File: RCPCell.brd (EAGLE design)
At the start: 99.8 x 44.5 mm, 18 parts, among them IC1 SIM900, U1 PESDXS4UD

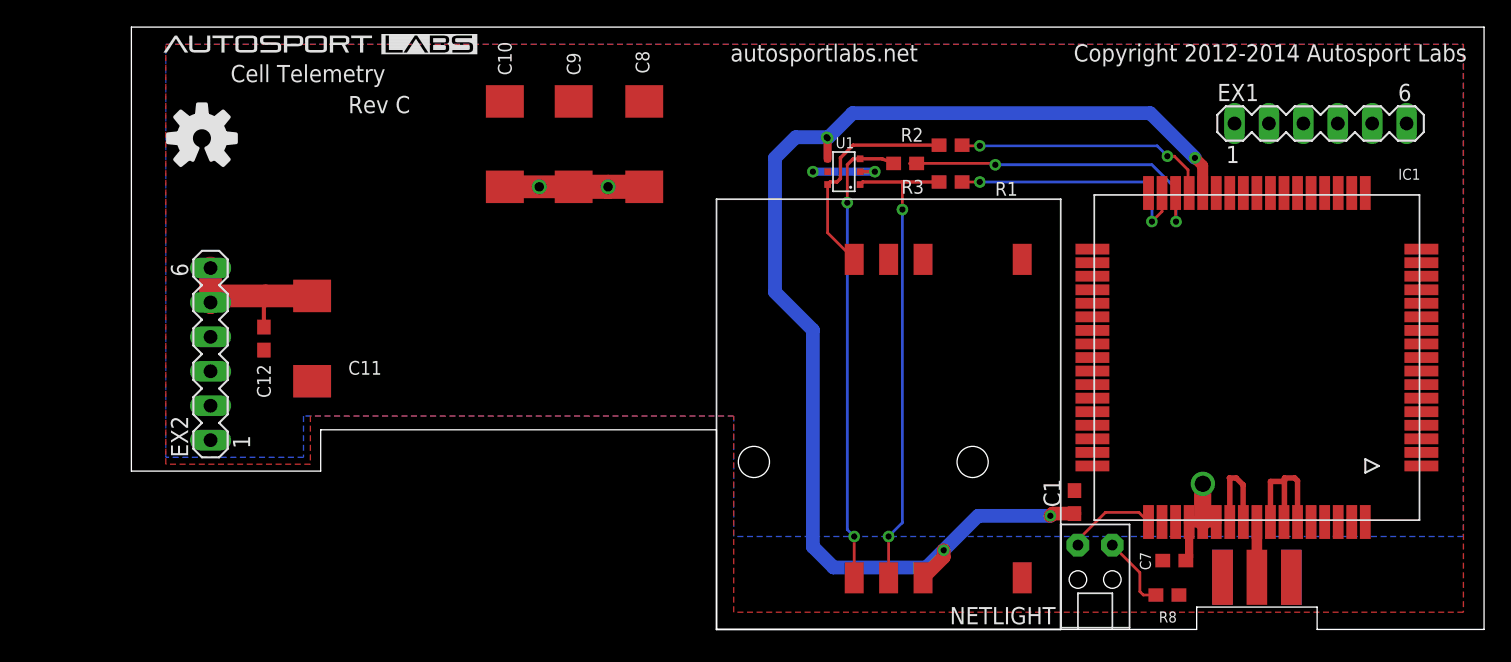
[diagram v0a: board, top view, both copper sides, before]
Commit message: laid out power supply section, fixed DRC errors
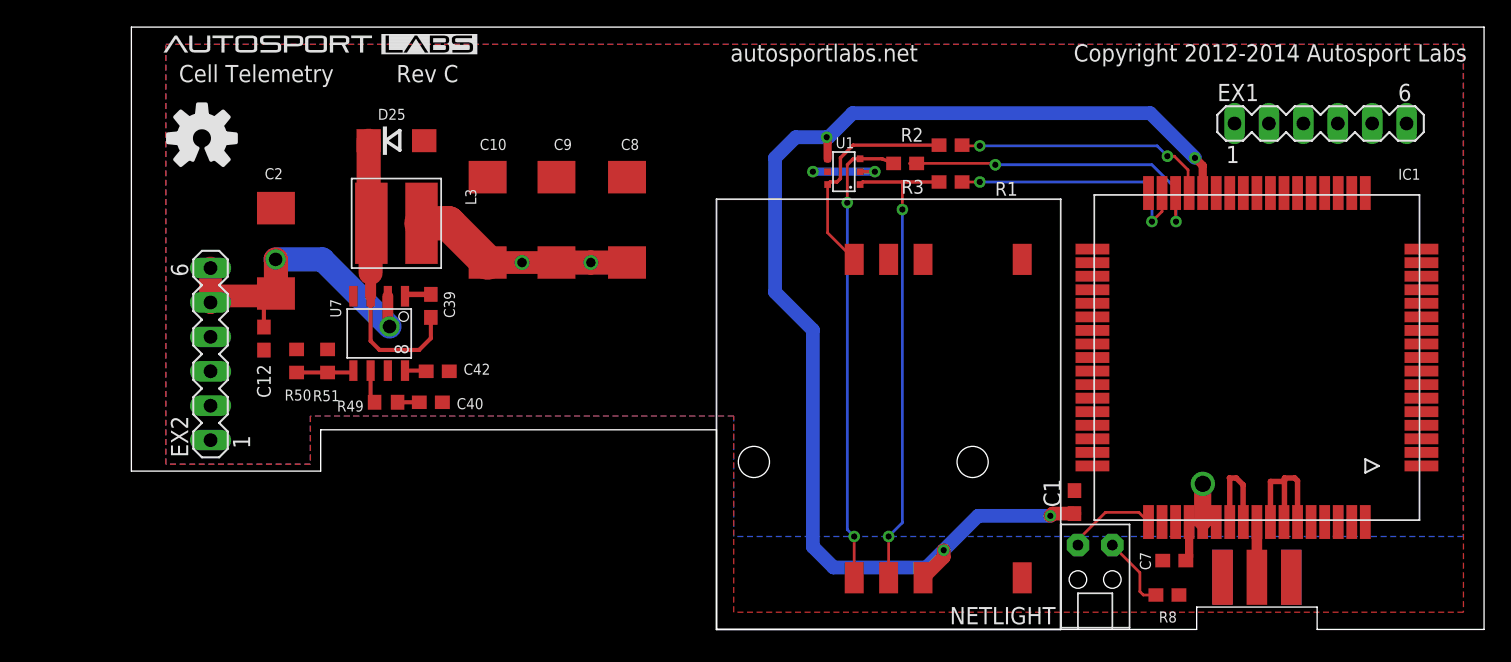
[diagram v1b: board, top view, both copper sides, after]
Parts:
- removed C11: 47uF, rcl:SMC_D
- added C2: 47uF, rcl:SMC_D
- added C39, C42: 0.01uF, rcl:C0603
- added C40: 560pF, rcl:C0603
- added D25: SCHOTTKY, smt_diodes:SMA
- added L3: CD54, sumida_inductors:CD54
- added R49: 43K, rcl:R0603
- added R50: 24K 1%, rcl:R0603
- added R51: 2.43K 1%, rcl:R0603
- added U7: FAN8303, voltage_regulators:SO-8
- moved C9 5.73 mm to (31.4, 30.2)
- moved C10 5.73 mm to (26.3, 30.2)
- moved C8 5.73 mm to (36.6, 30.2)
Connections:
- new net +6V: R50.1
- new net N$1000: C39.1, D25.C, L3.P$2, U7.3
- new net N$1100: C40.2, R49.2
- new net N$1200: R49.1, U7.6
- new net N$1300: C42.2, U7.8
- new net N$800: R50.2, R51.1, U7.5
- new net N$900: C39.2, U7.1
- net GND: now also C2.-, C40.1, C42.1, D25.A, R51.2, U7.4; no longer C11.-
- net SAFE12V: now also C2.+, U7.2; no longer C11.+
- net V+: now also L3.P$1
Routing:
- net N$1000: track 0.00 -> 21.5 mm
- net SAFE12V: track 12.6 -> 24.4 mm, vias 0 -> 2
- net V+: track 20.6 -> 26.4 mm
- net N$800: track 0.00 -> 4.25 mm
- net N$1200: track 0.00 -> 2.46 mm
- net N$900: track 0.00 -> 1.96 mm
- net N$1100: track 0.00 -> 1.60 mm
- net N$1300: track 0.00 -> 1.58 mm
- net SIM_VDD: track 92.2 -> 92.3 mm, vias 5 -> 4

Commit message: tentative final version of RevC module
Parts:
- added R4: 1k, SparkFun:0603
- moved C2 0.76 mm to (11.4, 27.9)
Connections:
- removed net +5V: EX2.3, EX2.4
- removed net PWRKEY_OUT: IC1.2
- removed net RXD3: EX1.6
- removed net TXD3: EX1.5
- new net EXT_CTRL: EX1.2, R4.2
- net DIN: now also EX1.5
- net DOUT: now also EX1.6
- net PWRKEY: now also R4.1
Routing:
- net PWRKEY: track 0.00 -> 35.1 mm, vias 0 -> 2
- net DOUT: track 0.00 -> 25.2 mm, vias 0 -> 1
- net DIN: track 0.00 -> 19.2 mm, vias 0 -> 1
- net EXT_CTRL: track 0.00 -> 3.32 mm
- net SAFE12V: track 24.4 -> 26.0 mm
- net GND: vias 2 -> 4
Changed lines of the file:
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@@
 </element>
 <element name="L3" library="sumida_inductors" package="CD54" value="CD54" x="19.558" y="29.972" rot="R270"/>
-<element name="C2" library="rcl" package="SMC_D" value="47uF" x="10.668" y="27.94" smashed="yes" rot="R90">
-<attribute name="NAME" x="11.176" y="34.036" size="0.8128" layer="25" rot="R180"/>
+<element name="C2" library="rcl" package="SMC_D" value="47uF" x="11.43" y="27.94" smashed="yes" rot="R90">
+<attribute name="NAME" x="11.938" y="34.036" size="0.8128" layer="25" rot="R180"/>
+</element>
+<element name="R4" library="SparkFun" package="0603" value="1k" x="84.836" y="40.64" smashed="yes" rot="R180">
+<attribute name="NAME" x="90.043" y="41.148" size="0.8128" layer="25" font="vector" rot="R180"/>
 </element>
 </elements>
@@
 <contactref element="C2" pad="-"/>
 <contactref element="C12" pad="2"/>
-<wire x1="85.598" y1="3.8481" x2="85.598" y2="3.8481" width="0" layer="19" extent="1-16"/>
-<wire x1="80.518" y1="3.8481" x2="80.518" y2="3.8481" width="0" layer="19" extent="1-16"/>
+<via x="80.518" y="3.81" extent="1-16" drill="0.4572"/>
+<via x="85.598" y="3.81" extent="1-16" drill="0.4572"/>
+<wire x1="80.518" y1="3.8481" x2="80.518" y2="3.81" width="0.254" layer="16"/>
+<wire x1="85.598" y1="3.8481" x2="85.598" y2="3.81" width="0.254" layer="16"/>
 </signal>
 <signal name="DIN">
 <contactref element="IC1" pad="10"/>
+<contactref element="EX1" pad="5"/>
+<wire x1="95.197" y1="21.066" x2="95.181" y2="21.082" width="0.254" layer="1"/>
+<wire x1="95.181" y1="21.082" x2="92.71" y2="21.082" width="0.254" layer="1"/>
+<via x="92.71" y="21.082" extent="1-16" drill="0.4572"/>
+<wire x1="92.71" y1="21.082" x2="91.567" y2="22.225" width="0.254" layer="16"/>
+<wire x1="91.567" y1="22.225" x2="91.567" y2="37.338" width="0.254" layer="16"/>
 </signal>
 <signal name="DOUT">
 <contactref element="IC1" pad="9"/>
+<contactref element="EX1" pad="6"/>
+<wire x1="94.107" y1="37.338" x2="95.197" y2="36.248" width="0.254" layer="16"/>
+<wire x1="95.197" y1="36.248" x2="95.197" y2="20.066" width="0.254" layer="16"/>
+<wire x1="95.197" y1="20.066" x2="91.44" y2="20.066" width="0.254" layer="16"/>
+<via x="91.44" y="20.066" extent="1-16" drill="0.4572"/>
+<wire x1="91.44" y1="20.066" x2="95.197" y2="20.066" width="0.254" layer="1"/>
 </signal>
 <signal name="V+" class="1">
@@
 <contactref element="IC1" pad="57"/>
 <contactref element="IC1" pad="56"/>
-<wire x1="36.7284" y1="27.0764" x2="36.703" y2="27.1018" width="1.778" layer="1"/>
 <wire x1="78.058" y1="5.326" x2="78.058" y2="7.927" width="0.6096" layer="1"/>
 <via x="79.0702" y="10.7442" extent="1-16" drill="1.2"/>
 <polygon width="0.4064" layer="16">
-<vertex x="44.45" y="6.858"/>
+<vertex x="44.45" y="1.27"/>
 <vertex x="44.45" y="15.748"/>
 <vertex x="13.208" y="15.748"/>
@@
 <vertex x="98.298" y="43.18"/>
 <vertex x="98.298" y="6.858"/>
+<vertex x="68.072" y="6.858"/>
+<vertex x="68.072" y="1.27"/>
 </polygon>
 <wire x1="79.0702" y1="10.7442" x2="79.058" y2="10.732" width="0.8128" layer="1"/>
@@
 <wire x1="23.393" y1="29.972" x2="26.289" y2="27.076" width="2.54" layer="1"/>
 <wire x1="78.058" y1="5.326" x2="77.812" y2="5.08" width="0" layer="19" extent="1-1"/>
-<wire x1="36.7284" y1="27.0764" x2="36.576" y2="27.076" width="0" layer="19" extent="1-1"/>
-</signal>
-<signal name="+5V">
-<contactref element="EX2" pad="3"/>
-<contactref element="EX2" pad="4"/>
-<wire x1="5.842" y1="19.05" x2="5.842" y2="21.59" width="0" layer="19" extent="1-1"/>
 </signal>
 <signal name="RF_ANT">
@@
 <signal name="PWRKEY">
 <contactref element="IC1" pad="1"/>
-</signal>
-<signal name="PWRKEY_OUT">
-<contactref element="IC1" pad="2"/>
+<contactref element="R4" pad="1"/>
+<wire x1="85.686" y1="40.64" x2="87.376" y2="40.64" width="0.254" layer="1"/>
+<via x="87.376" y="40.64" extent="1-16" drill="0.4572"/>
+<wire x1="87.376" y1="40.64" x2="87.757" y2="40.259" width="0.254" layer="16"/>
+<wire x1="87.757" y1="40.259" x2="87.757" y2="34.925" width="0.254" layer="16"/>
+<wire x1="87.757" y1="34.925" x2="89.916" y2="32.766" width="0.254" layer="16"/>
+<wire x1="89.916" y1="32.766" x2="89.916" y2="14.732" width="0.254" layer="16"/>
+<wire x1="89.916" y1="14.732" x2="92.71" y2="11.938" width="0.254" layer="16"/>
+<wire x1="92.71" y1="11.938" x2="93.218" y2="11.938" width="0.254" layer="16"/>
+<via x="93.218" y="11.938" extent="1-16" drill="0.4572"/>
+<wire x1="93.218" y1="11.938" x2="93.346" y2="12.066" width="0.254" layer="1"/>
+<wire x1="93.346" y1="12.066" x2="95.197" y2="12.066" width="0.254" layer="1"/>
 </signal>
 <signal name="STATUS">
@@
 <via x="59.944" y="5.842" extent="1-16" drill="0.4572"/>
 <wire x1="59.944" y1="5.842" x2="62.484" y2="8.382" width="1.016" layer="16"/>
-<wire x1="62.484" y1="8.382" x2="67.818" y2="8.382" width="1.016" layer="16"/>
-<via x="67.818" y="8.382" extent="1-16" drill="0.4572"/>
-<wire x1="67.818" y1="8.382" x2="67.984" y2="8.548" width="1.016" layer="1"/>
-<wire x1="67.984" y1="8.548" x2="69.596" y2="8.548" width="1.016" layer="1"/>
+<wire x1="62.484" y1="8.382" x2="66.802" y2="8.382" width="1.016" layer="16"/>
+<via x="66.802" y="8.382" extent="1-16" drill="0.4572"/>
+<wire x1="66.802" y1="8.382" x2="66.968" y2="8.548" width="1.016" layer="1"/>
+<wire x1="66.968" y1="8.548" x2="69.596" y2="8.548" width="1.016" layer="1"/>
 <wire x1="79.058" y1="32.205" x2="79.058" y2="34.226" width="0.6096" layer="1"/>
 <wire x1="79.058" y1="34.226" x2="78.486" y2="34.798" width="0.6096" layer="1"/>
@@
 <wire x1="5.842" y1="24.13" x2="5.842" y2="26.67" width="1.6764" layer="1"/>
 <wire x1="5.842" y1="24.13" x2="6.325" y2="24.613" width="1.6764" layer="1"/>
-<wire x1="6.325" y1="24.613" x2="9.906" y2="24.613" width="1.6764" layer="1"/>
-<wire x1="9.779" y1="22.313" x2="9.779" y2="24.486" width="0.3048" layer="1"/>
-<wire x1="9.779" y1="24.486" x2="9.906" y2="24.613" width="0.3048" layer="1"/>
+<wire x1="6.325" y1="24.613" x2="10.668" y2="24.613" width="1.6764" layer="1"/>
+<wire x1="10.541" y1="24.486" x2="10.668" y2="24.613" width="0.3048" layer="1"/>
 <contactref element="U7" pad="2"/>
 <contactref element="C2" pad="+"/>
-<wire x1="10.668" y1="24.79" x2="10.668" y2="27.2796" width="1.778" layer="1"/>
-<wire x1="10.668" y1="27.2796" x2="10.6426" y2="27.305" width="1.778" layer="1"/>
-<via x="10.6426" y="27.305" extent="1-16" drill="1"/>
-<wire x1="10.6426" y1="27.305" x2="14.097" y2="27.305" width="1.778" layer="16"/>
+<wire x1="11.43" y1="24.79" x2="11.43" y2="27.2796" width="1.778" layer="1"/>
+<wire x1="11.43" y1="27.2796" x2="11.4046" y2="27.305" width="1.778" layer="1"/>
+<via x="11.4046" y="27.305" extent="1-16" drill="1"/>
+<wire x1="11.4046" y1="27.305" x2="14.097" y2="27.305" width="1.778" layer="16"/>
 <wire x1="14.097" y1="27.305" x2="19.05" y2="22.352" width="1.778" layer="16"/>
 <via x="19.05" y="22.352" extent="1-16" drill="1"/>
 <wire x1="19.05" y1="22.352" x2="18.923" y2="22.479" width="0.8128" layer="1"/>
 <wire x1="18.923" y1="22.479" x2="18.923" y2="24.5872" width="0.8128" layer="1"/>
-<wire x1="9.906" y1="24.613" x2="10.668" y2="24.79" width="0" layer="19" extent="1-1"/>
-</signal>
-<signal name="TXD3">
-<contactref element="EX1" pad="5"/>
-</signal>
-<signal name="RXD3">
-<contactref element="EX1" pad="6"/>
+<wire x1="9.779" y1="22.313" x2="9.906" y2="22.44" width="0.254" layer="1"/>
+<wire x1="9.906" y1="22.44" x2="9.906" y2="23.368" width="0.254" layer="1"/>
+<wire x1="9.906" y1="23.368" x2="11.151" y2="24.613" width="0.254" layer="1"/>
+<wire x1="11.328" y1="24.79" x2="11.43" y2="24.79" width="0.254" layer="1"/>
+<wire x1="11.328" y1="24.79" x2="11.151" y2="24.613" width="0.254" layer="1"/>
+<wire x1="11.151" y1="24.613" x2="10.668" y2="24.613" width="0.254" layer="1"/>
 </signal>
 <signal name="USB_DM_HS_OUT">
@@
 <contactref element="R50" pad="1"/>
 </signal>
+<signal name="EXT_CTRL">
+<contactref element="EX1" pad="2"/>
+<contactref element="R4" pad="2"/>
+<wire x1="83.947" y1="37.338" x2="83.986" y2="37.377" width="0.254" layer="1"/>
+<wire x1="83.986" y1="37.377" x2="83.986" y2="40.64" width="0.254" layer="1"/>
+</signal>
 </signals>

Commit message: yak shaving design a bit
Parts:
- R51: value 2.43K 1% -> 3.9K 1%
- moved D25 1.02 mm to (19.6, 35.1)
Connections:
- net GND renamed N$2
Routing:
- net N$2: track 24.3 -> 34.7 mm
- net N$1000: track 21.5 -> 20.5 mm

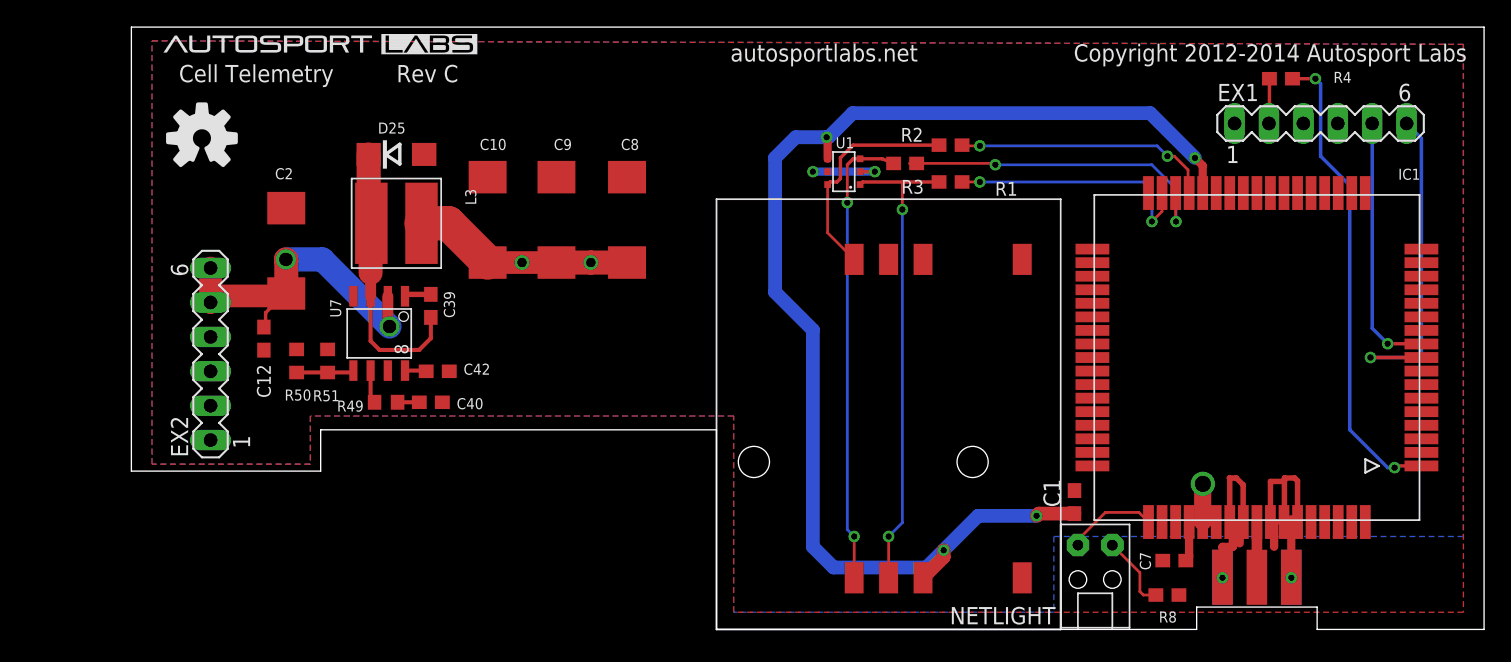
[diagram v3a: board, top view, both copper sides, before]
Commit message: WIP for flipping cell module components over
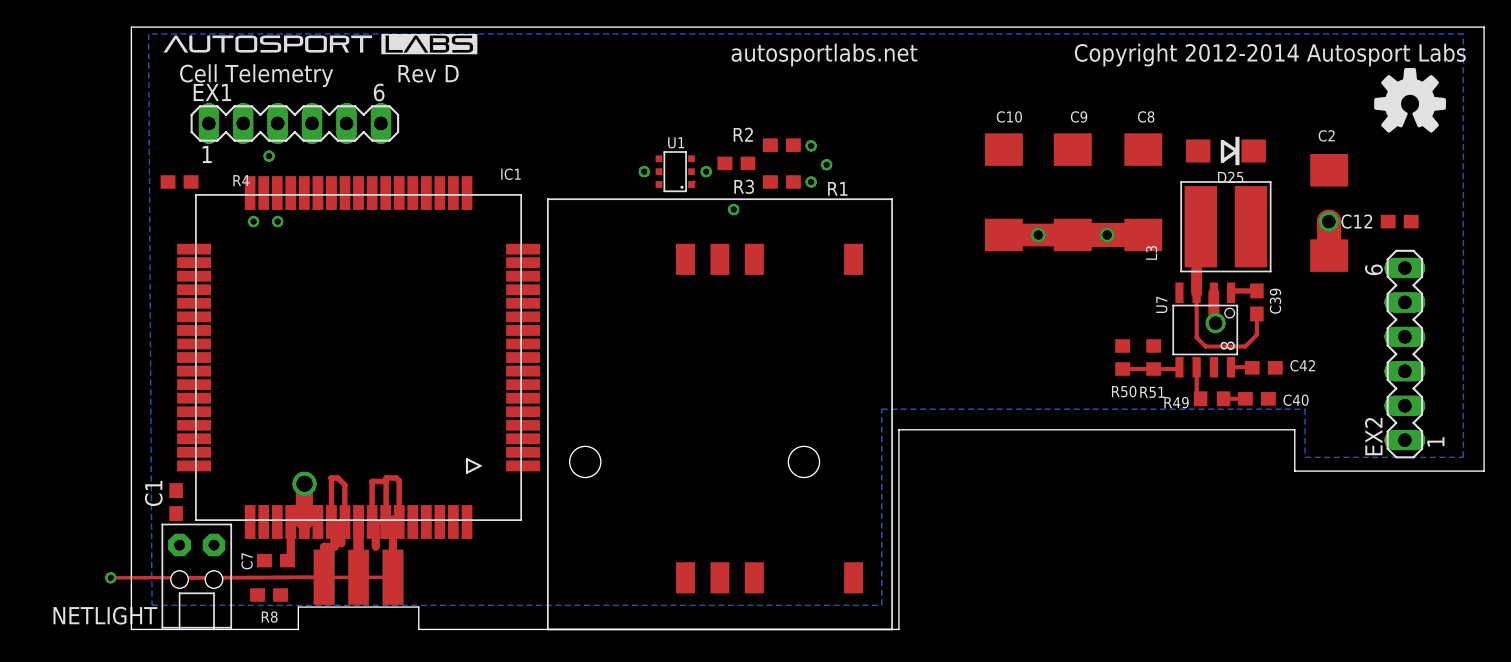
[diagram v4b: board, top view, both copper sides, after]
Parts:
- moved EX2 88.1 mm to (94.0, 20.3)
- moved C12 84.3 mm to (93.6, 30.1), turned to 180 degrees
- moved R4 81.6 mm to (3.56, 33.0)
- moved C2 77.0 mm to (88.4, 30.7)
- moved EX1 75.7 mm to (12.1, 37.3)
- moved C7 66.3 mm to (10.7, 5.08)
- moved IC1 66.3 mm to (16.8, 20.1)
- moved NETLIGHT 66.3 mm to (4.83, 4.57)
- moved C1 66.3 mm to (3.30, 9.40)
- moved J$1 66.3 mm to (14.2, 3.85)
- moved R8 66.3 mm to (10.2, 2.54)
- moved D25 61.2 mm to (80.8, 35.3), turned to 180 degrees
- moved L3 61.2 mm to (80.8, 29.7), turned to 90 degrees
- moved C39 61.0 mm to (83.1, 24.1)
- moved C40 61.0 mm to (83.1, 17.0)
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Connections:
- removed net +6V: R50.1
- new net GND: C10.-, C12.2, C2.-, C40.1, C42.1, C7.2, C8.-, C9.-, D25.A, R51.2, U7.4
- net N$2: now also U$1.3; no longer C10.-, C12.2, C2.-, C40.1, C42.1, C7.2, C8.-, C9.-, D25.A, R51.2, U$1.6, U7.4
- net SIM_CLK_CARD: now also U$1.6; no longer U$1.3
- net SIM_DATA_CARD: now also U$1.1; no longer U$1.4
- net SIM_RST_CARD: now also U$1.5; no longer U$1.2
- net SIM_VDD: now also U$1.4; no longer U$1.1
- net V+: now also R50.1
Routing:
- net SIM_VDD: track 92.3 -> 0.00 mm, vias 4 -> 0
- net SIM_RST_CARD: track 35.5 -> 0.27 mm, vias 2 -> 1
- net PWRKEY: track 35.1 -> 0.00 mm, vias 2 -> 0
- net SIM_CLK_CARD: track 34.4 -> 0.00 mm, vias 2 -> 0
- net N$2: track 34.7 -> 60.5 mm
- net DOUT: track 25.2 -> 0.00 mm, vias 1 -> 0
- net SIM_CLK: track 25.0 -> 0.00 mm
- net SAFE12V: track 26.0 -> 4.81 mm
- net DIN: track 19.2 -> 0.00 mm, vias 1 -> 0
- net SIM_DATA: track 19.2 -> 0.00 mm
- net SIM_RST: track 19.0 -> 0.00 mm
- net SIM_DATA_CARD: track 16.7 -> 0.00 mm
- net N$1000: track 20.5 -> 11.6 mm
- net STATUS: track 6.72 -> 0.00 mm
- net V+: track 26.3 -> 20.3 mm
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- added copper zone on layer 16, net N$2
- removed copper zone on layer 1, net N$2
- removed copper zone on layer 16, net V+
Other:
- outline, holes or cut-outs redrawn
- board text added: "Rev D"
- board text removed: "Rev C"
